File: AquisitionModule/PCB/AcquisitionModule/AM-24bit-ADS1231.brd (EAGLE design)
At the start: 160 x 100 mm, 7 parts, among them IC1 LM336LP, U1 ADS1231ID, X1 bridge_conn, X2 43160-1104

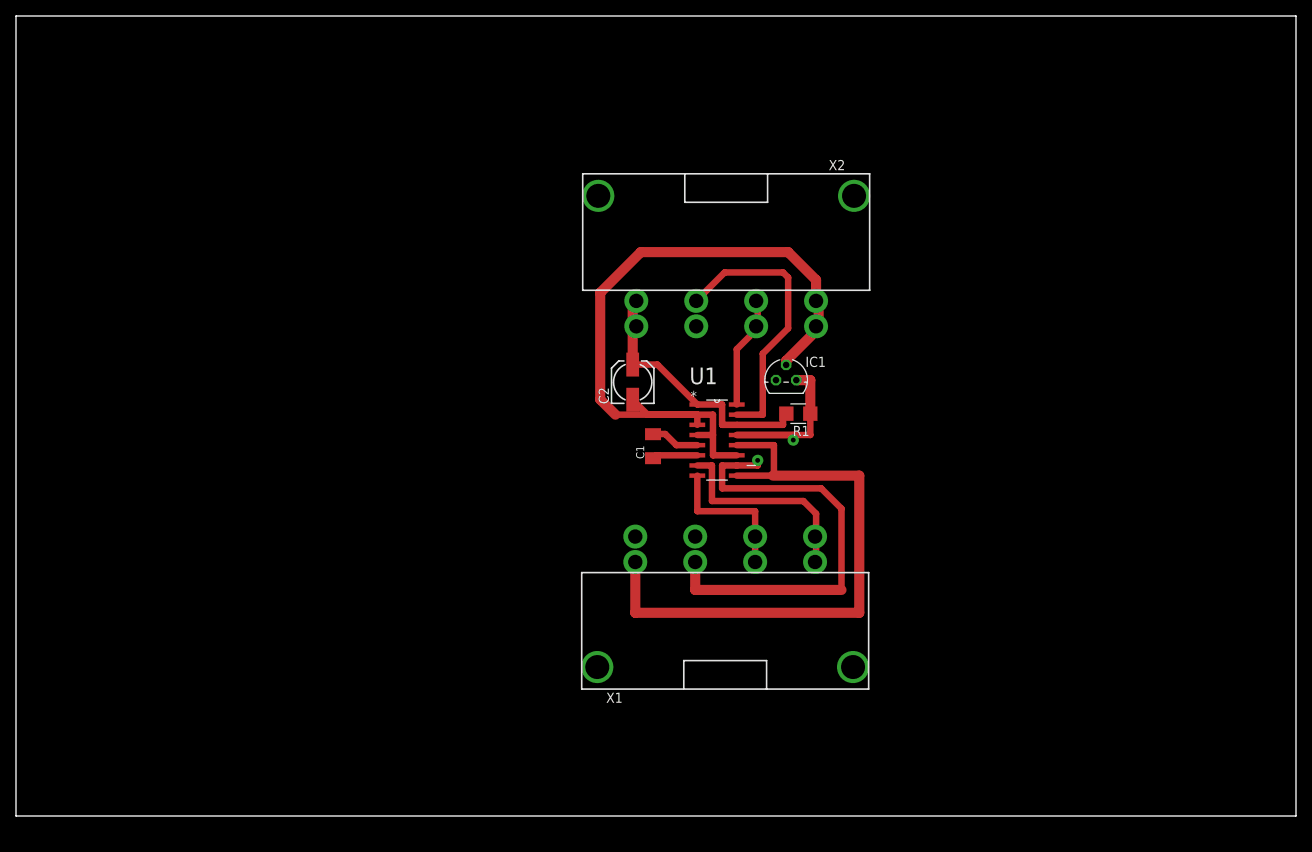
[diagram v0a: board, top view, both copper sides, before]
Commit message: Added routes on PCB between Molex connector via and thickening the existing one..
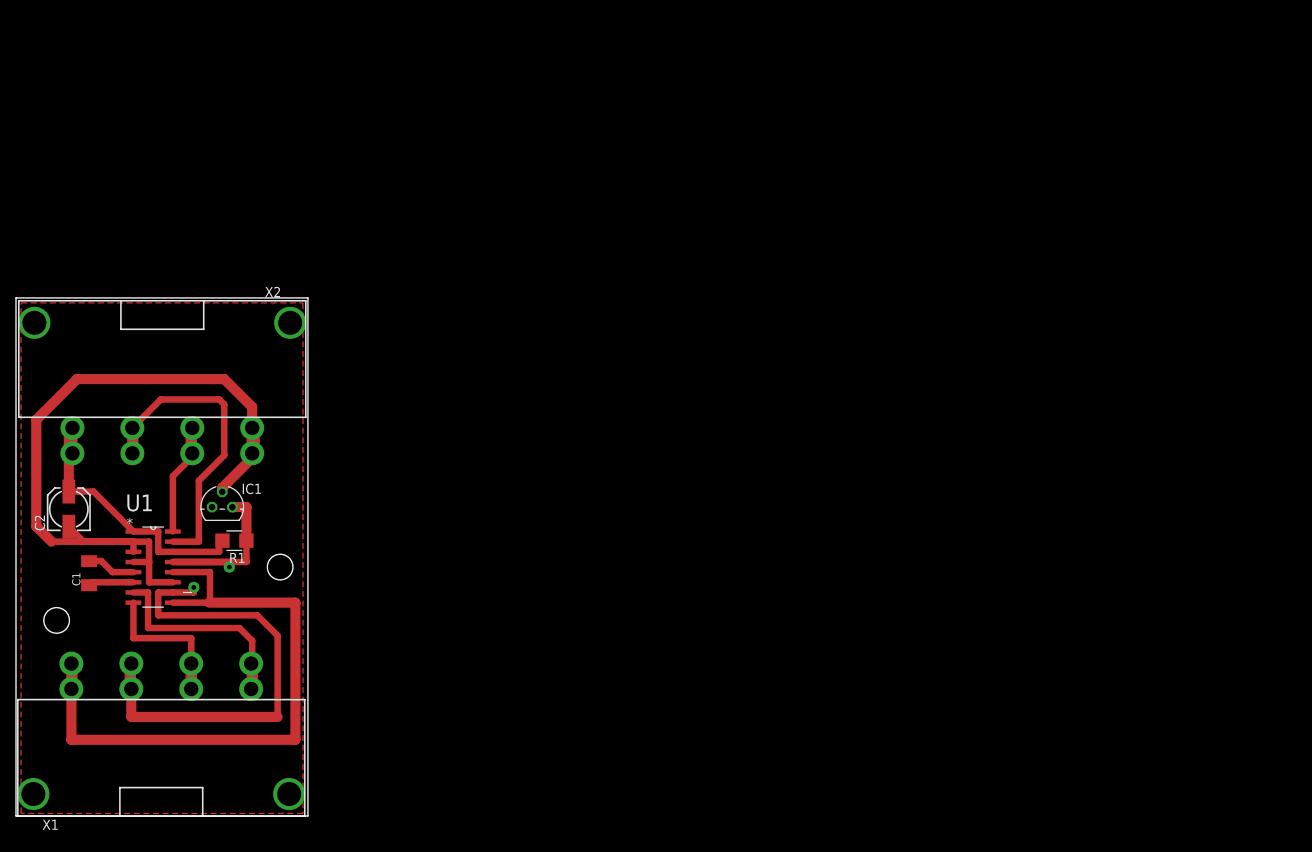
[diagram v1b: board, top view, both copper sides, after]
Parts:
- moved IC1 72.3 mm to (25.8, 38.6)
- moved R1 72.3 mm to (27.3, 34.4)
- moved C1 72.3 mm to (9.14, 30.4)
- moved C2 72.3 mm to (6.60, 38.4)
- moved U1 72.3 mm to (17.1, 31.1)
- moved X1 72.3 mm to (18.2, 15.9)
- moved X2 72.3 mm to (18.3, 48.5)
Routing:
- net N$12: track 0.00 -> 4.45 mm
- net N$5: track 18.0 -> 21.8 mm
- net N$4: track 26.0 -> 29.8 mm
- net N$11: track 0.00 -> 3.81 mm
- net N$14: track 0.00 -> 3.49 mm
- net N$16: track 0.00 -> 3.17 mm
- net N$15: track 0.00 -> 3.17 mm
- net N$13: track 0.00 -> 3.17 mm
- added copper zone on layer 1, net N$10
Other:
- board size 160 x 100 mm -> 36.5 x 64.8 mm
